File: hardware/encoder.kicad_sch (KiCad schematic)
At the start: 2 parts, among them U401 MT6835

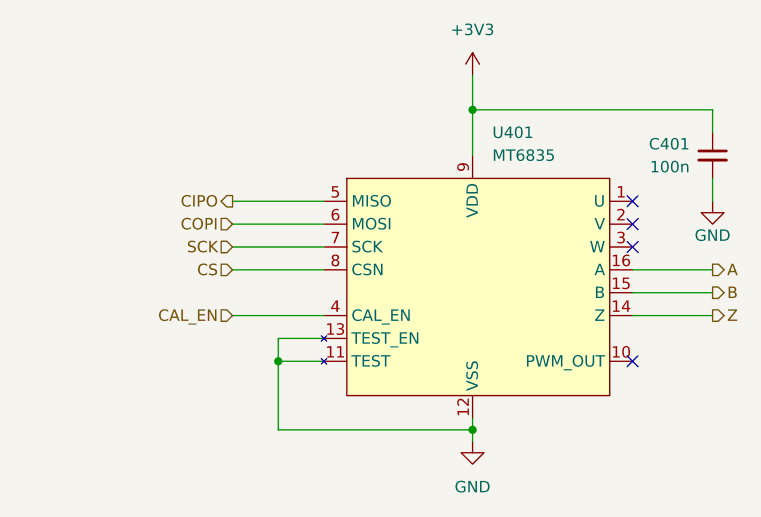
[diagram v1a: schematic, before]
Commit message: rework power plane
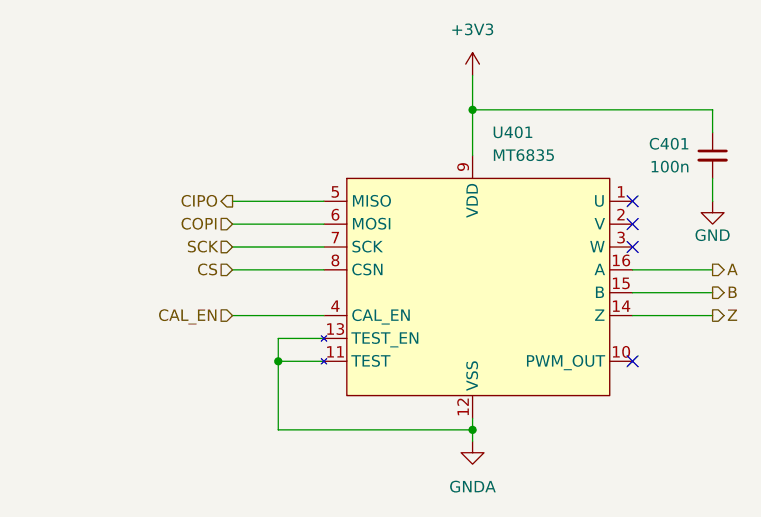
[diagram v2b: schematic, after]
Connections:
- net GND: no longer U401.11 (TEST), U401.12 (VSS), U401.13 (TEST_EN)
- new net GNDA: U401.11 (TEST), U401.12 (VSS), U401.13 (TEST_EN)
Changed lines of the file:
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@@
     )
   )
-  (symbol (lib_id "power:GND") (at 146.05 110.49 0) (unit 1)
+  (symbol (lib_id "power:GNDA") (at 146.05 110.49 0) (unit 1)
     (in_bom yes) (on_board yes) (dnp no) (fields_autoplaced)
-    (property "Reference" "#PWR0402" (at 146.05 116.84 0)
+    (property "Reference" "#PWR0710" (at 146.05 116.84 0)
       (effects (font (size 1.27 1.27)) hide)
     )
-    (property "Value" "GND" (at 146.05 115.57 0)
+    (property "Value" "GNDA" (at 146.05 115.57 0)
       (effects (font (size 1.27 1.27)))
     )
@@
     (instances
       (project "lemon-pepper"
+        (path "/0306e2fa-4433-4288-91d9-65a3484207ad/41d11f3b-333a-47c0-a126-1f991ee11e83"
+          (reference "#PWR0710") (unit 1)
+        )
         (path "/0306e2fa-4433-4288-91d9-65a3484207ad/e3a86f21-c1c7-4a99-9511-7bc9966878a0"
           (reference "#PWR0402") (unit 1)

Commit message: work on analog layout
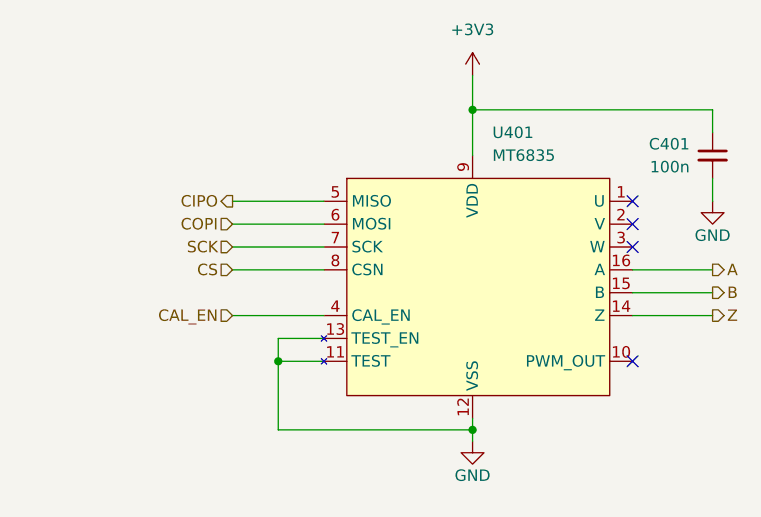
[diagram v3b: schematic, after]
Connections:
- net GNDA is gone; now on net GND: U401.11 (TEST), U401.12 (VSS), U401.13 (TEST_EN)
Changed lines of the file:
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@@
     (effects (font (size 1.27 1.27)) (justify right))
+  )
+  (symbol (lib_id "power:GND") (at 146.05 110.49 0) (unit 1)
+    (in_bom yes) (on_board yes) (dnp no)
+    (property "Reference" "#PWR0402" (at 146.05 116.84 0)
+      (effects (font (size 1.27 1.27)) hide)
+    )
+    (property "Value" "GND" (at 146.05 114.3 0)
+      (effects (font (size 1.27 1.27)))
+    )
+    (property "Footprint" "" (at 146.05 110.49 0)
+      (effects (font (size 1.27 1.27)) hide)
+    )
+    (property "Datasheet" "" (at 146.05 110.49 0)
+      (effects (font (size 1.27 1.27)) hide)
+    )
+    (pin "1")
+    (instances
+      (project "lemon-pepper"
+        (path "/0306e2fa-4433-4288-91d9-65a3484207ad/e3a86f21-c1c7-4a99-9511-7bc9966878a0"
+          (reference "#PWR0402") (unit 1)
+        )
+      )
+    )
   )
   (symbol (lib_id "power:GND") (at 172.72 83.82 0) (unit 1)
@@
         )
       )
-    )
-  )
-  (symbol (lib_id "power:GNDA") (at 146.05 110.49 0) (unit 1)
-    (in_bom yes) (on_board yes) (dnp no) (fields_autoplaced)
-    (property "Reference" "#PWR0710" (at 146.05 116.84 0)
-      (effects (font (size 1.27 1.27)) hide)
-    )
-    (property "Value" "GNDA" (at 146.05 115.57 0)
-      (effects (font (size 1.27 1.27)))
-    )
-    (property "Footprint" "" (at 146.05 110.49 0)
-      (effects (font (size 1.27 1.27)) hide)
-    )
-    (property "Datasheet" "" (at 146.05 110.49 0)
-      (effects (font (size 1.27 1.27)) hide)
-    )
-    (pin "1")
-    (instances
-      (project "lemon-pepper"
-        (path "/0306e2fa-4433-4288-91d9-65a3484207ad/41d11f3b-333a-47c0-a126-1f991ee11e83"
-          (reference "#PWR0710") (unit 1)
-        )
-        (path "/0306e2fa-4433-4288-91d9-65a3484207ad/e3a86f21-c1c7-4a99-9511-7bc9966878a0"
-          (reference "#PWR0402") (unit 1)
-        )
-      )

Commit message: clean up ERC in schematic
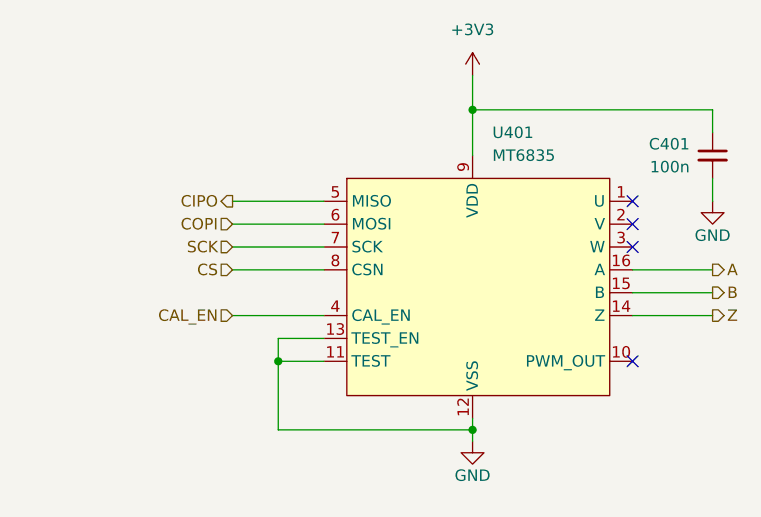
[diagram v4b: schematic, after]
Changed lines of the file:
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@@
     (pin "1")
     (pin "10")
-    (pin "11")
-    (pin "13")
     (pin "14")
     (pin "15")
@@
     (pin "7")
     (pin "8")
+    (pin "11")
     (pin "12")
+    (pin "13")
     (pin "9")
     (instances

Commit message: fix bringup issues
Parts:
- added R?: 10k, Resistor_SMD:R_0402_1005Metric, symbol Device:R_Small_US
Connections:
- net +3V3: now also R?.1
- net CS: now also R?.2
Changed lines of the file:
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@@
   (junction (at 146.05 73.66) (diameter 0) (color 0 0 0 0)
+  )
+  (junction (at 107.95 91.44) (diameter 0) (color 0 0 0 0)
   )
   (junction (at 124.46 101.6) (diameter 0) (color 0 0 0 0)
@@
     (stroke (width 0) (type default))
   )
+  (wire (pts (xy 107.95 88.9) (xy 107.95 91.44))
+    (stroke (width 0) (type default))
+  )
   (wire (pts (xy 119.38 83.82) (xy 129.54 83.82))
     (stroke (width 0) (type default))
   )
-  (wire (pts (xy 119.38 91.44) (xy 129.54 91.44))
+  (wire (pts (xy 100.33 91.44) (xy 107.95 91.44))
     (stroke (width 0) (type default))
   )
@@
     (stroke (width 0) (type default))
   )
+  (wire (pts (xy 107.95 91.44) (xy 129.54 91.44))
+    (stroke (width 0) (type default))
+  )
   (wire (pts (xy 119.38 96.52) (xy 129.54 96.52))
     (stroke (width 0) (type default))
@@
   )
   (wire (pts (xy 124.46 101.6) (xy 124.46 109.22))
+    (stroke (width 0) (type default))
+  )
+  (wire (pts (xy 107.95 81.28) (xy 107.95 83.82))
     (stroke (width 0) (type default))
   )
@@
     (effects (font (size 1.27 1.27)) (justify right))
   )
-  (hierarchical_label "CS" (shape input) (at 119.38 91.44 180) (fields_autoplaced)
+  (hierarchical_label "CS" (shape input) (at 100.33 91.44 180) (fields_autoplaced)
     (effects (font (size 1.27 1.27)) (justify right))
   )
@@
     )
   )
+  (symbol (lib_id "Device:R_Small_US") (at 107.95 86.36 0) (mirror y) (unit 1)
+    (in_bom yes) (on_board yes) (dnp no)
+    (property "Reference" "R?" (at 105.41 85.09 0)
+      (effects (font (size 1.27 1.27)) (justify left))
+    )
+    (property "Value" "10k" (at 105.41 87.63 0)
+      (effects (font (size 1.27 1.27)) (justify left))
+    )
+    (property "Footprint" "Resistor_SMD:R_0402_1005Metric" (at 107.95 86.36 0)
+      (effects (font (size 1.27 1.27)) hide)
+    )
+    (property "Datasheet" "~" (at 107.95 86.36 0)
+      (effects (font (size 1.27 1.27)) hide)
+    )
+    (property "LCSC Part" "C25744" (at 107.95 86.36 0)
+      (effects (font (size 1.27 1.27)) hide)
+    )
+    (pin "1")
+    (pin "2")
+    (instances
+      (project "lemon-pepper"
+        (path "/0306e2fa-4433-4288-91d9-65a3484207ad/7f2d245a-6dca-4eb9-9839-7fdf255edd98"
+          (reference "R?") (unit 1)
+        )
+        (path "/0306e2fa-4433-4288-91d9-65a3484207ad/e3a86f21-c1c7-4a99-9511-7bc9966878a0"
+          (reference "R401") (unit 1)
+        )
+      )
+      (project "stm32g431-mt6701-stspin233"
+        (path "/bcb2c98d-7159-437a-9ffb-b81c5fcc4307"
+          (reference "R?") (unit 1)
+        )
+        (path "/bcb2c98d-7159-437a-9ffb-b81c5fcc4307/ed84ebbf-b2e5-4959-b495-bf58cd9b4c8c"
+          (reference "R203") (unit 1)
+        )
+      )
+    )
+  )
   (symbol (lib_id "Device:C_Small") (at 172.72 78.74 0) (unit 1)
     (in_bom yes) (on_board yes) (dnp no)
@@
         )
       )
+    )
+  )
+  (symbol (lib_id "power:+3V3") (at 107.95 81.28 0) (unit 1)
+    (in_bom yes) (on_board yes) (dnp no) (fields_autoplaced)
+    (property "Reference" "#PWR0313" (at 107.95 85.09 0)
+      (effects (font (size 1.27 1.27)) hide)
+    )
+    (property "Value" "+3V3" (at 107.95 76.2 0)
+      (effects (font (size 1.27 1.27)))
+    )
+    (property "Footprint" "" (at 107.95 81.28 0)
+      (effects (font (size 1.27 1.27)) hide)
+    )
+    (property "Datasheet" "" (at 107.95 81.28 0)
+      (effects (font (size 1.27 1.27)) hide)
+    )
+    (pin "1")
+    (instances
+      (project "lemon-pepper"
+        (path "/0306e2fa-4433-4288-91d9-65a3484207ad/7f2d245a-6dca-4eb9-9839-7fdf255edd98"
+          (reference "#PWR0313") (unit 1)
+        )
+        (path "/0306e2fa-4433-4288-91d9-65a3484207ad/e3a86f21-c1c7-4a99-9511-7bc9966878a0"
+          (reference "#PWR0404") (unit 1)
+        )
+      )
+      (project "stm32g431-mt6701-stspin233"
+        (path "/bcb2c98d-7159-437a-9ffb-b81c5fcc4307"
+          (reference "#PWR0107") (unit 1)
+        )
+        (path "/bcb2c98d-7159-437a-9ffb-b81c5fcc4307/ed84ebbf-b2e5-4959-b495-bf58cd9b4c8c"
+          (reference "#PWR0203") (unit 1)
+        )
+      )

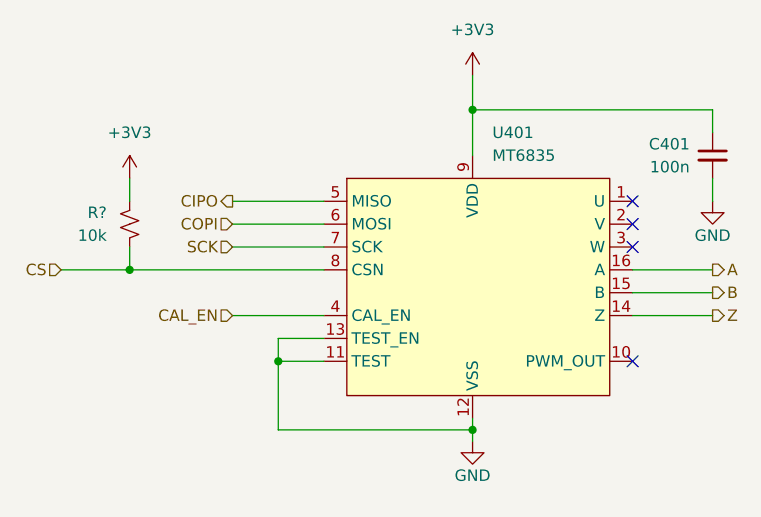
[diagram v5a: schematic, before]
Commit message: Update firmware defines to match hardware
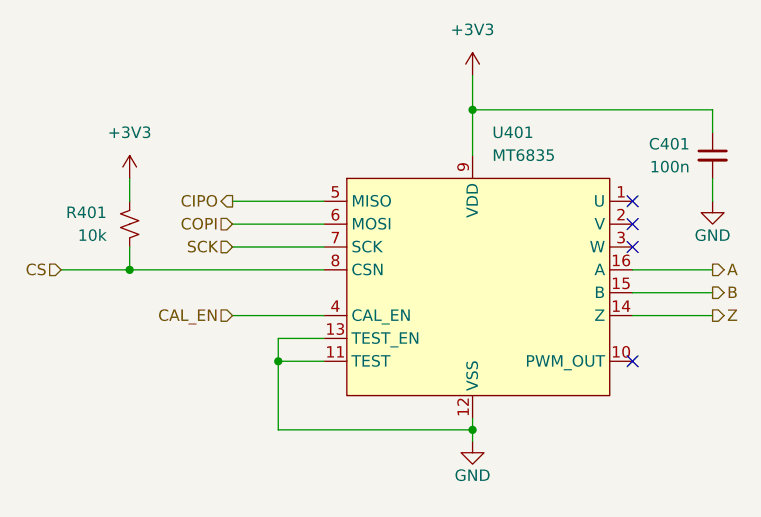
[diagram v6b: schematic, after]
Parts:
- gave numbers to parts that had none: 1
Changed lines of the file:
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@@
   (symbol (lib_id "Device:R_Small_US") (at 107.95 86.36 0) (mirror y) (unit 1)
     (in_bom yes) (on_board yes) (dnp no)
-    (property "Reference" "R?" (at 105.41 85.09 0)
+    (property "Reference" "R401" (at 105.41 85.09 0)
       (effects (font (size 1.27 1.27)) (justify left))
     )
@@
     (instances
       (project "lemon-pepper"
-        (path "/0306e2fa-4433-4288-91d9-65a3484207ad/7f2d245a-6dca-4eb9-9839-7fdf255edd98"
-          (reference "R?") (unit 1)
-        )
         (path "/0306e2fa-4433-4288-91d9-65a3484207ad/e3a86f21-c1c7-4a99-9511-7bc9966878a0"
           (reference "R401") (unit 1)
@@
   (symbol (lib_id "power:+3V3") (at 107.95 81.28 0) (unit 1)
     (in_bom yes) (on_board yes) (dnp no) (fields_autoplaced)
-    (property "Reference" "#PWR0313" (at 107.95 85.09 0)
+    (property "Reference" "#PWR0404" (at 107.95 85.09 0)
       (effects (font (size 1.27 1.27)) hide)
     )
@@
     (instances
       (project "lemon-pepper"
-        (path "/0306e2fa-4433-4288-91d9-65a3484207ad/7f2d245a-6dca-4eb9-9839-7fdf255edd98"
-          (reference "#PWR0313") (unit 1)
-        )
         (path "/0306e2fa-4433-4288-91d9-65a3484207ad/e3a86f21-c1c7-4a99-9511-7bc9966878a0"
           (reference "#PWR0404") (unit 1)

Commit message: Update BOM field LCSC ID
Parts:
- C401: LCSC ID (none) -> C307331; LCSC Part C307331 -> (none)
- R401: LCSC ID (none) -> C25744; LCSC Part C25744 -> (none)
- U401: LCSC ID (none) -> C2932578; LCSC Part C2932578 -> (none)
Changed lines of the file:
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@@
 			)
 		)
-		(property "LCSC Part" "C25744"
+		(property "LCSC ID" "C25744"
 			(at 107.95 86.36 0)
 			(effects
@@
 			)
 		)
-		(property "LCSC Part" "C307331"
+		(property "LCSC ID" "C307331"
 			(at 172.72 78.74 0)
 			(effects
@@
 			)
 		)
-		(property "LCSC Part" "C2932578"
-			(at 146.05 96.52 0)
-			(effects
+		(property "LCSC ID" "C2932578"
+			(at 146.05 96.52 0)
+			(effects
